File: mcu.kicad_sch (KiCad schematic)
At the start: 16 parts, among them SW301 Reset, SW302 Boot, SW303 SW, U301 ESP32-S3-WROOM-1-N8

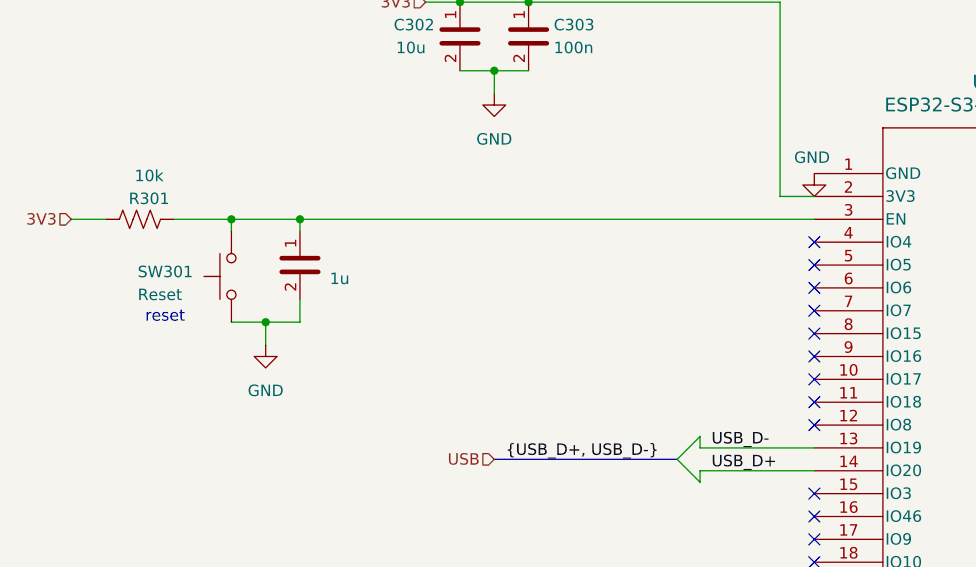
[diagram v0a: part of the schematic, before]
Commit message: change size
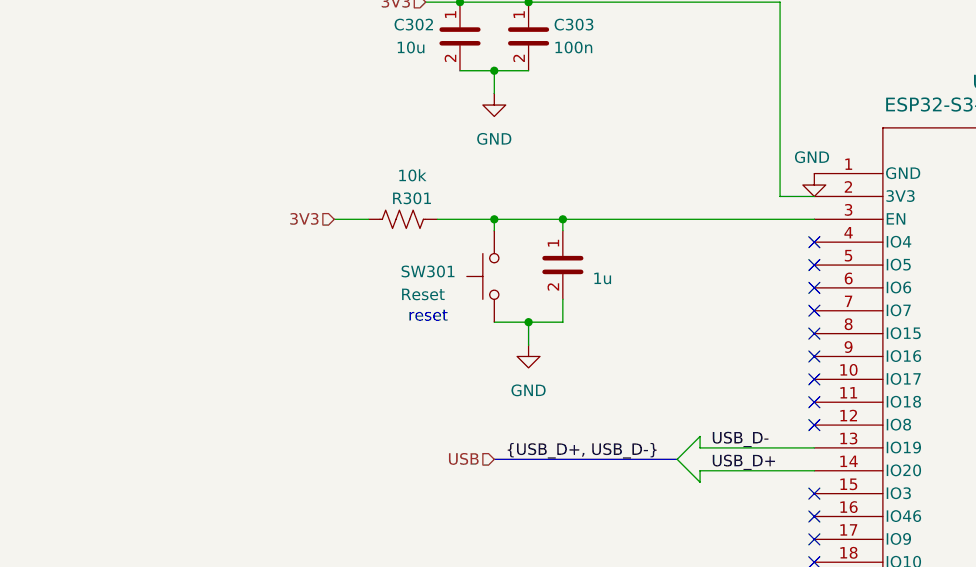
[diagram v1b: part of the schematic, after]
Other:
- moved on the sheet: R301, SW301

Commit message: updated layout (usb/buttons), generated gerbers
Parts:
- removed SW301: Reset, Button_Switch_SMD:SW_Push_SPST_NO_Alps_SKRK, symbol bfr_actuators:Generic_Pushbutton
- removed SW302: Boot, Button_Switch_SMD:SW_Push_SPST_NO_Alps_SKRK, symbol bfr_actuators:Generic_Pushbutton
- removed SW303: SW, Button_Switch_SMD:SW_Push_SPST_NO_Alps_SKRK, symbol bfr_actuators:Generic_Pushbutton
- added S301, S302, S303: TS-1088-AR02016, TS-1088-AR02016:SW_TS-1088-AR02016, symbol TS-1088-AR02016:TS-1088-AR02016
- renumbered C302 to C301, C303 to C302, C301 to C303, R305 to R302, R304 to R303, R303 to R304, R302 to R305
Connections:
- net GND: now also S301.1, S302.2, S303.1
- net at R302.1, U301.27 (IO0): now also S303.2
- net at C304.1, U301.32 (IO39): now also S302.1
- net at C303.1, R301.2, U301.3 (EN): now also S301.2

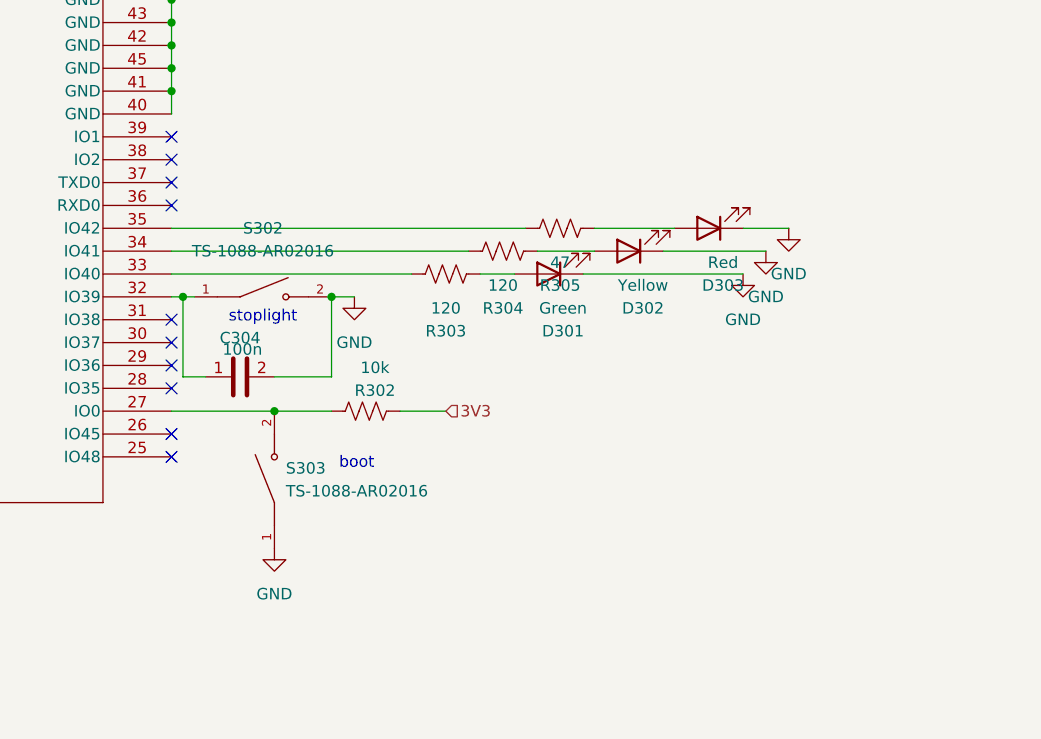
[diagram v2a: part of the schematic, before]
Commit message: added button pullup + mounting holes
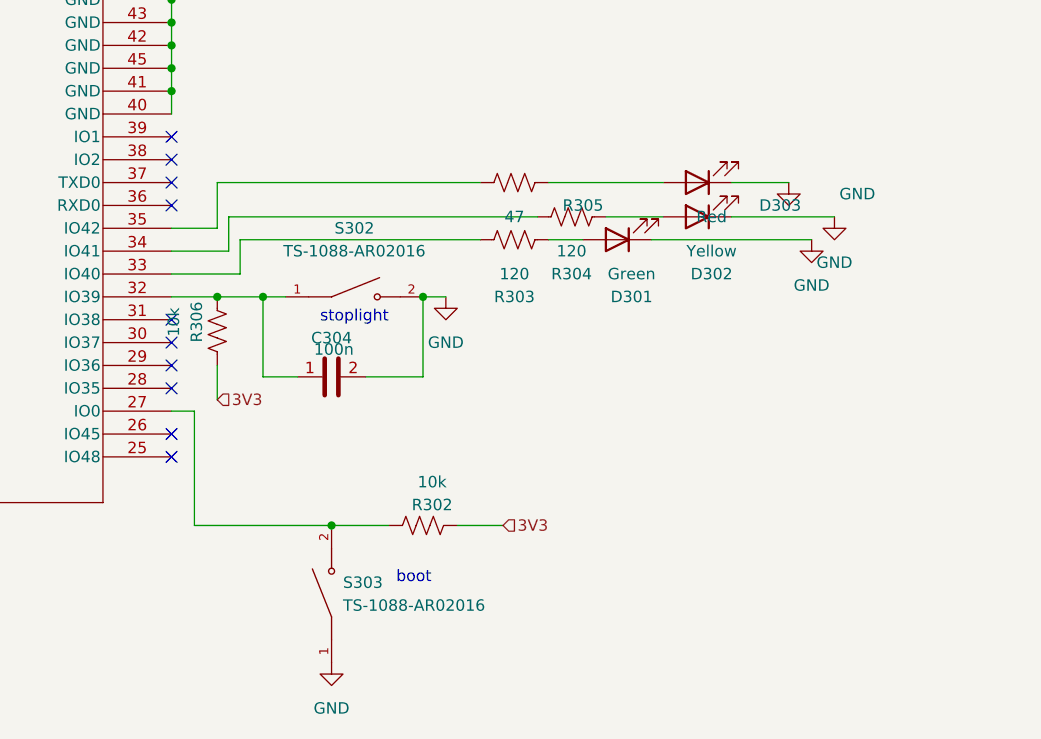
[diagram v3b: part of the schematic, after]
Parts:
- added R306: 10k, Resistor_SMD:R_0603_1608Metric_Pad0.98x0.95mm_HandSolder, symbol bfr_resistors:RMCF0603FT10K0
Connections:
- net 3V3: now also R306.1
- net at C304.1, S302.1, U301.32 (IO39): now also R306.2
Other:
- moved on the sheet: C304, D301, D302, D303, R302, R303, R304, R305, S302, S303

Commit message: changed battery
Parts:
- renumbered D303 to D302, D302 to D303, R306 to R302, R302 to R303, R305 to R304, R303 to R305, R304 to R306, S303 to S302, S302 to S303
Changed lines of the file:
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@@
 		(dnp no)
 		(fields_autoplaced yes)
-		(property "Reference" "D302"
+		(property "Reference" "D303"
 			(at 206.0575 109.22 0)
 			(show_name no)
@@
 			(project "watt_city_stoplight_pcb"
 				(path "/b4a4f794-1678-4879-8515-a84d8e78c2b5/3dd86ff8-e3bb-420d-8a24-6450469b82c4"
-					(reference "D302")
+					(reference "D303")
 					(unit 1)
 				)
@@
 		(in_pos_files yes)
 		(dnp no)
-		(property "Reference" "R306"
+		(property "Reference" "R302"
 			(at 148.844 114.554 0)
 			(show_name no)
@@
 			(project "watt_city_stoplight_pcb"
 				(path "/b4a4f794-1678-4879-8515-a84d8e78c2b5/3dd86ff8-e3bb-420d-8a24-6450469b82c4"
-					(reference "R306")
+					(reference "R302")
 					(unit 1)
 				)
@@
 		(dnp no)
 		(fields_autoplaced yes)
-		(property "Reference" "R304"
+		(property "Reference" "R306"
 			(at 190.5 109.22 0)
 			(show_name no)
@@
 			(project "watt_city_stoplight_pcb"
 				(path "/b4a4f794-1678-4879-8515-a84d8e78c2b5/3dd86ff8-e3bb-420d-8a24-6450469b82c4"
-					(reference "R304")
+					(reference "R306")
 					(unit 1)
 				)
@@
 		(in_pos_files yes)
 		(dnp no)
-		(property "Reference" "R302"
+		(property "Reference" "R303"
 			(at 175.006 134.874 0)
 			(show_name no)
@@
 			(project "watt_city_stoplight_pcb"
 				(path "/b4a4f794-1678-4879-8515-a84d8e78c2b5/3dd86ff8-e3bb-420d-8a24-6450469b82c4"
-					(reference "R302")
+					(reference "R303")
 					(unit 1)
 				)
@@
 		(in_pos_files yes)
 		(dnp no)
-		(property "Reference" "R305"
+		(property "Reference" "R304"
 			(at 191.77 101.6 0)
 			(show_name no)
@@
 			(project "watt_city_stoplight_pcb"
 				(path "/b4a4f794-1678-4879-8515-a84d8e78c2b5/3dd86ff8-e3bb-420d-8a24-6450469b82c4"
-					(reference "R305")
+					(reference "R304")
 					(unit 1)
 				)
@@
 		(dnp no)
 		(fields_autoplaced yes)
-		(property "Reference" "S303"
+		(property "Reference" "S302"
 			(at 165.1 143.5099 90)
 			(show_name no)
@@
 			(project "watt_city_stoplight_pcb"
 				(path "/b4a4f794-1678-4879-8515-a84d8e78c2b5/3dd86ff8-e3bb-420d-8a24-6450469b82c4"
-					(reference "S303")
+					(reference "S302")
 					(unit 1)
 				)
@@
 		(dnp no)
 		(fields_autoplaced yes)
-		(property "Reference" "#PWR0307"
+		(property "Reference" "#PWR0308"
 			(at 217.17 111.76 0)
 			(hide yes)
@@
 			(project "watt_city_stoplight_pcb"
 				(path "/b4a4f794-1678-4879-8515-a84d8e78c2b5/3dd86ff8-e3bb-420d-8a24-6450469b82c4"
-					(reference "#PWR0307")
+					(reference "#PWR0308")
 					(unit 1)
 				)
@@
 		(in_pos_files yes)
 		(dnp no)
-		(property "Reference" "D303"
+		(property "Reference" "D302"
 			(at 213.6775 101.6 0)
 			(show_name no)
@@
 			(project "watt_city_stoplight_pcb"
 				(path "/b4a4f794-1678-4879-8515-a84d8e78c2b5/3dd86ff8-e3bb-420d-8a24-6450469b82c4"
-					(reference "D303")
+					(reference "D302")
 					(unit 1)
 				)
@@
 		(in_pos_files yes)
 		(dnp no)
-		(property "Reference" "#PWR0309"
+		(property "Reference" "#PWR0307"
 			(at 214.63 105.41 0)
 			(hide yes)
@@
 			(project "watt_city_stoplight_pcb"
 				(path "/b4a4f794-1678-4879-8515-a84d8e78c2b5/3dd86ff8-e3bb-420d-8a24-6450469b82c4"
-					(reference "#PWR0309")
+					(reference "#PWR0307")
 					(unit 1)
 				)
@@
 		(dnp no)
 		(fields_autoplaced yes)
-		(property "Reference" "R303"
+		(property "Reference" "R305"
 			(at 184.15 111.76 0)
 			(show_name no)
@@
 			(project "watt_city_stoplight_pcb"
 				(path "/b4a4f794-1678-4879-8515-a84d8e78c2b5/3dd86ff8-e3bb-420d-8a24-6450469b82c4"
-					(reference "R303")
+					(reference "R305")
 					(unit 1)
 				)
@@
 		(dnp no)
 		(fields_autoplaced yes)
-		(property "Reference" "S302"
+		(property "Reference" "S303"
 			(at 166.37 104.14 0)
 			(show_name no)
@@
 			(project "watt_city_stoplight_pcb"
 				(path "/b4a4f794-1678-4879-8515-a84d8e78c2b5/3dd86ff8-e3bb-420d-8a24-6450469b82c4"
-					(reference "S302")
+					(reference "S303")
 					(unit 1)
 				)
@@
 		(dnp no)
 		(fields_autoplaced yes)
-		(property "Reference" "#PWR0308"
+		(property "Reference" "#PWR0309"
 			(at 219.71 109.22 0)
 			(hide yes)
@@
 			(project "watt_city_stoplight_pcb"
 				(path "/b4a4f794-1678-4879-8515-a84d8e78c2b5/3dd86ff8-e3bb-420d-8a24-6450469b82c4"
-					(reference "#PWR0308")
+					(reference "#PWR0309")
 					(unit 1)
 				)
